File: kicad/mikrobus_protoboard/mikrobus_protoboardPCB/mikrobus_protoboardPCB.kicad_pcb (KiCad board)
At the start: 2 copper layers, 25.2 x 57.2 mm, 0 parts

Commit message: nets complete
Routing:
- net GND: track 0.00 -> 100.9 mm, vias 0 -> 17
- net 5V: track 0.00 -> 36.1 mm, vias 0 -> 8
- net 3V3: track 0.00 -> 36.0 mm, vias 0 -> 8
- net SDA: track 0.00 -> 7.69 mm, vias 0 -> 4
- net TX: track 0.00 -> 7.62 mm, vias 0 -> 4
- net SCL: track 0.00 -> 7.62 mm, vias 0 -> 4
- net SCK: track 0.00 -> 7.62 mm, vias 0 -> 4
- net RX: track 0.00 -> 7.62 mm, vias 0 -> 4
- net RST: track 0.00 -> 7.62 mm, vias 0 -> 4
- net PWD: track 0.00 -> 7.62 mm, vias 0 -> 4
- net MOSI: track 0.00 -> 7.62 mm, vias 0 -> 4
- net MISO: track 0.00 -> 7.62 mm, vias 0 -> 4
- net INT: track 0.00 -> 7.62 mm, vias 0 -> 4
- net CS: track 0.00 -> 7.62 mm, vias 0 -> 4
- net AN: track 0.00 -> 7.62 mm, vias 0 -> 4
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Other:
- board size 25.2 x 57.2 mm -> 25.8 x 57.5 mm

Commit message: protoboard ready
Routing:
- net GND: track 100.9 -> 0.37 mm
- added copper zone on F.Cu, net GND
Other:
- board size 25.8 x 57.5 mm -> 26.8 x 57.5 mm
- board text added: "3.3V"
- board text added: "5V"
- board text added: "AN"
- board text added: "CS"
- board text added: "GND"
- board text added: "INT"
- board text added: "PWD"
- board text added: "RST"
- board text added: "RX"
- board text added: "SCK"
- board text added: "SCL"
- board text added: "SDA"
- board text added: "SDI"
- board text added: "SDO"
- board text added: "TX"

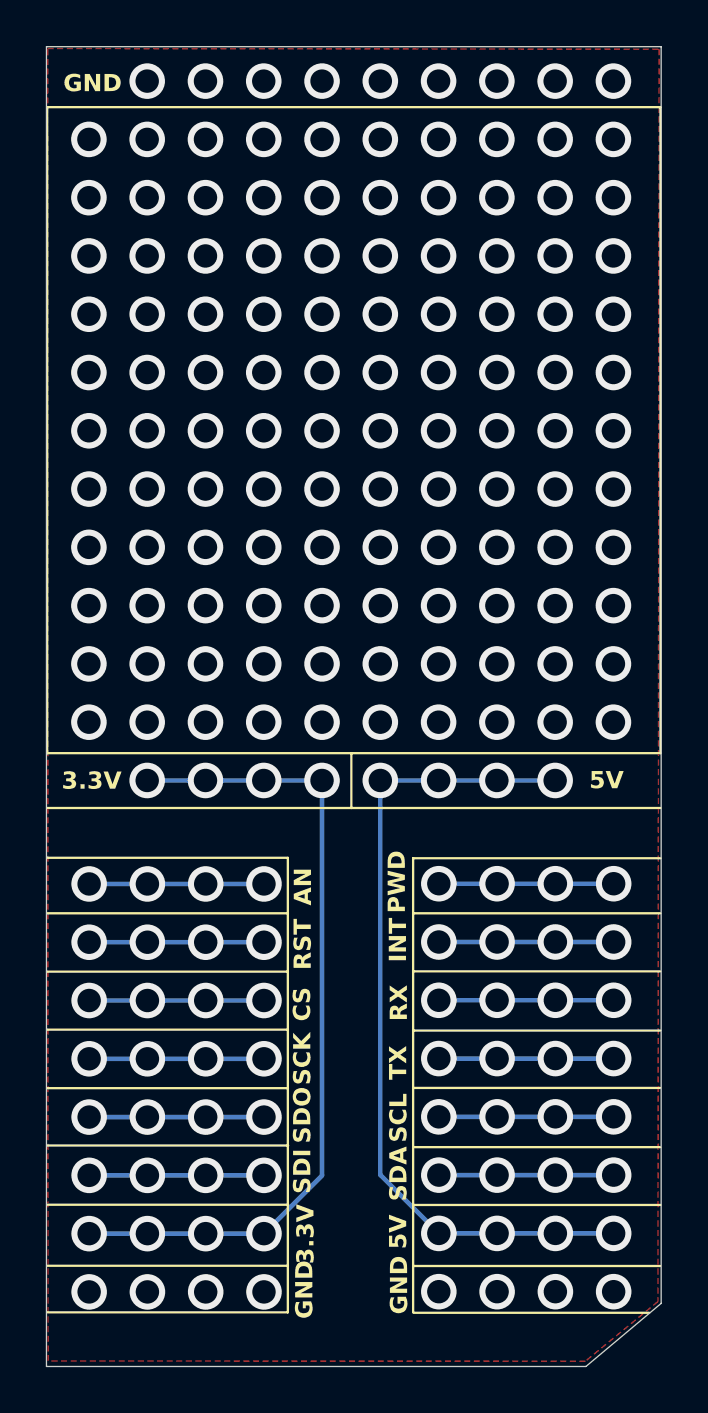
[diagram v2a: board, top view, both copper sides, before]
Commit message: MikroBUS logo added
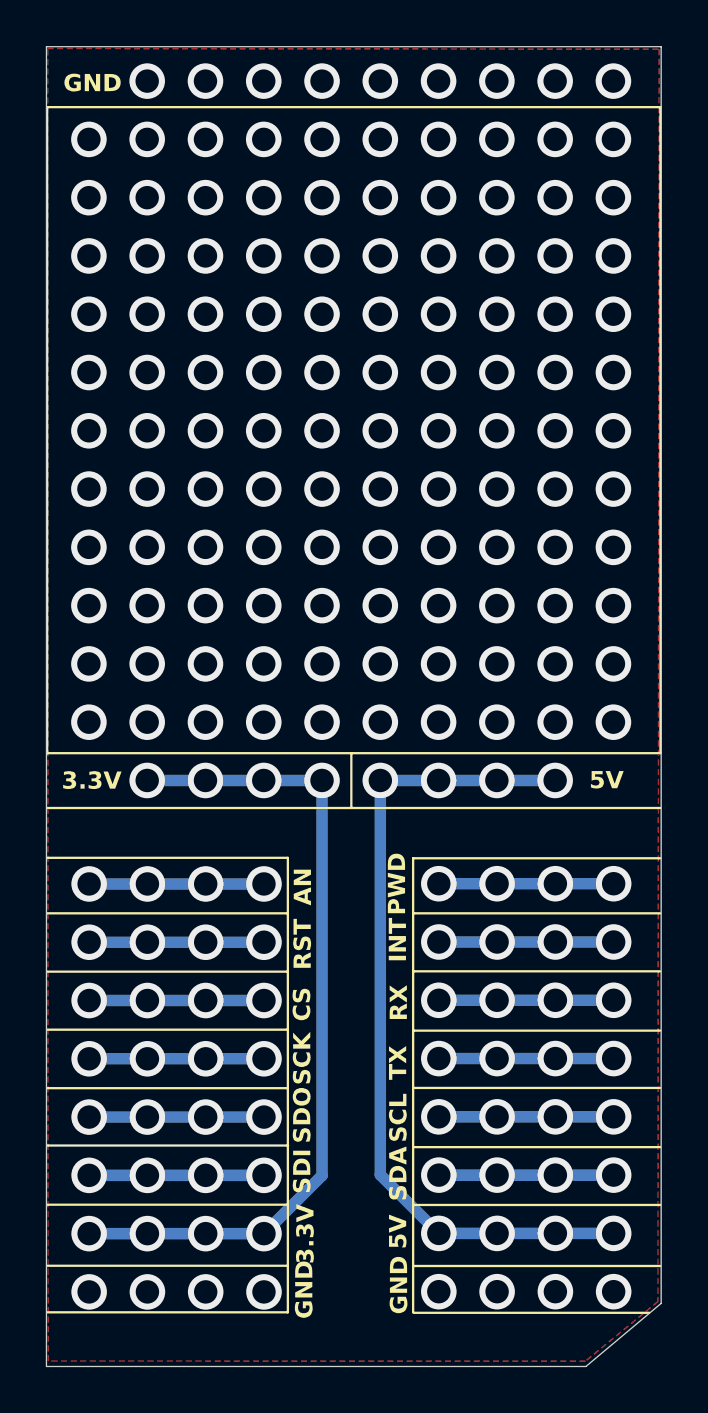
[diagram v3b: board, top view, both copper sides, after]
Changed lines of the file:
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@@
 	)
 	(gr_text "PWD"
-		(at 163.6 86.59 90)
+		(at 163.61 86.68 90)
 		(layer "F.SilkS")
 		(effects
@@
 		(start 164.98 103.09)
 		(end 164.99 103.08)
-		(width 0.2)
+		(width 0.5)
 		(layer "F.Cu")
 		(net 1)
@@
 		(start 164.75 103.08)
 		(end 164.99 103.08)
-		(width 0.2)
+		(width 0.5)
 		(layer "B.Cu")
 		(net 1)
@@
 		(start 164.87 103.08)
 		(end 164.99 103.08)
-		(width 0.2)
+		(width 0.5)
 		(layer "B.Cu")
 		(net 1)
@@
 		(start 159.9 98.02)
 		(end 157.37 100.55)
-		(width 0.2)
+		(width 0.5)
 		(layer "B.Cu")
 		(net 2)
@@
 		(start 154.82 80.8)
 		(end 157.36 80.8)
-		(width 0.2)
+		(width 0.5)
 		(layer "B.Cu")
 		(net 2)
@@
 		(start 157.37 100.55)
 		(end 154.83 100.55)
-		(width 0.2)
+		(width 0.5)
 		(layer "B.Cu")
 		(net 2)
@@
 		(start 152.29 100.55)
 		(end 149.75 100.55)
-		(width 0.2)
+		(width 0.5)
 		(layer "B.Cu")
 		(net 2)
@@
 		(start 154.83 100.55)
 		(end 152.29 100.55)
-		(width 0.2)
+		(width 0.5)
 		(layer "B.Cu")
 		(net 2)
@@
 		(start 152.28 80.8)
 		(end 154.82 80.8)
-		(width 0.2)
+		(width 0.5)
 		(layer "B.Cu")
 		(net 2)
@@
 		(start 157.36 80.8)
 		(end 159.9 80.8)
-		(width 0.2)
+		(width 0.5)
 		(layer "B.Cu")
 		(net 2)
@@
 		(start 159.9 80.8)
 		(end 159.9 98.02)
-		(width 0.2)
+		(width 0.5)
 		(layer "B.Cu")
 		(net 2)
@@
 		(start 172.61 100.54)
 		(end 172.59 100.54)
-		(width 0.2)
+		(width 0.5)
 		(layer "F.Cu")
 		(net 3)
@@
 		(start 172.59 100.54)
 		(end 172.57 100.52)
-		(width 0.2)
+		(width 0.5)
 		(layer "F.Cu")
 		(net 3)
@@
 		(start 172.57 100.52)
 		(end 172.55 100.54)
-		(width 0.2)
+		(width 0.5)
 		(layer "F.Cu")
 		(net 3)
@@
 		(start 162.44 80.8)
 		(end 164.98 80.8)
-		(width 0.2)
+		(width 0.5)
 		(layer "B.Cu")
 		(net 3)
@@
 		(start 167.53 100.54)
 		(end 170.07 100.54)
-		(width 0.2)
+		(width 0.5)
 		(layer "B.Cu")
 		(net 3)
@@
 		(start 170.07 100.54)
 		(end 172.61 100.54)
-		(width 0.2)
+		(width 0.5)
 		(layer "B.Cu")
 		(net 3)
@@
 		(start 164.99 100.54)
 		(end 167.53 100.54)
-		(width 0.2)
+		(width 0.5)
 		(layer "B.Cu")
 		(net 3)
@@
 		(start 167.52 80.8)
 		(end 170.06 80.8)
-		(width 0.2)
+		(width 0.5)
 		(layer "B.Cu")
 		(net 3)
@@
 		(start 162.44 97.99)
 		(end 164.99 100.54)
-		(width 0.2)
+		(width 0.5)
 		(layer "B.Cu")
 		(net 3)
@@
 		(start 164.98 80.8)
 		(end 167.52 80.8)
-		(width 0.2)
+		(width 0.5)
 		(layer "B.Cu")
 		(net 3)
@@
 		(start 162.44 80.8)
 		(end 162.44 97.99)
-		(width 0.2)
+		(width 0.5)
 		(layer "B.Cu")
 		(net 3)
@@
 		(start 167.53 85.3)
 		(end 170.07 85.3)
-		(width 0.2)
+		(width 0.5)
 		(layer "B.Cu")
 		(net 4)
@@
 		(start 164.99 85.3)
 		(end 167.53 85.3)
-		(width 0.2)
+		(width 0.5)
 		(layer "B.Cu")
 		(net 4)
@@
 		(start 170.07 85.3)
 		(end 172.61 85.3)
-		(width 0.2)
+		(width 0.5)
 		(layer "B.Cu")
 		(net 4)
@@
 		(start 164.99 87.84)
 		(end 167.53 87.84)
-		(width 0.2)
+		(width 0.5)
 		(layer "B.Cu")
 		(net 5)
@@
 		(start 167.53 87.84)
 		(end 170.07 87.84)
-		(width 0.2)
+		(width 0.5)
 		(layer "B.Cu")
 		(net 5)
@@
 		(start 170.07 87.84)
 		(end 172.61 87.84)
-		(width 0.2)
+		(width 0.5)
 		(layer "B.Cu")
 		(net 5)
@@
 		(start 167.53 90.38)
 		(end 170.07 90.38)
-		(width 0.2)
+		(width 0.5)
 		(layer "B.Cu")
 		(net 6)
@@
 		(start 164.99 90.38)
 		(end 167.53 90.38)
-		(width 0.2)
+		(width 0.5)
 		(layer "B.Cu")
 		(net 6)
@@
 		(start 170.07 90.38)
 		(end 172.61 90.38)
-		(width 0.2)
+		(width 0.5)
 		(layer "B.Cu")
 		(net 6)
@@
 		(start 172.61 92.92)
 		(end 170.07 92.92)
-		(width 0.2)
+		(width 0.5)
 		(layer "B.Cu")
 		(net 7)
@@
 		(start 167.53 92.92)
 		(end 164.99 92.92)
-		(width 0.2)
+		(width 0.5)
 		(layer "B.Cu")
 		(net 7)
@@
 		(start 170.07 92.92)
 		(end 167.53 92.92)
-		(width 0.2)
+		(width 0.5)
 		(layer "B.Cu")
 		(net 7)
@@
 		(start 164.99 95.46)
 		(end 167.53 95.46)
-		(width 0.2)
+		(width 0.5)
 		(layer "B.Cu")
 		(net 8)
@@
 		(start 172.61 95.46)
 		(end 170.07 95.46)
-		(width 0.2)
+		(width 0.5)
 		(layer "B.Cu")
 		(net 8)
@@
 		(start 167.53 95.46)
 		(end 170.07 95.46)
-		(width 0.2)
+		(width 0.5)
 		(layer "B.Cu")
 		(net 8)
@@
 		(start 167.57 98.04)
 		(end 167.53 98)
-		(width 0.2)
+		(width 0.5)
 		(layer "F.Cu")
 		(net 9)
@@
 		(start 170.07 98)
 		(end 170.07 98.03)
-		(width 0.2)
+		(width 0.5)
 		(layer "F.Cu")
 		(net 9)
@@
 		(start 170.07 98.03)
 		(end 170.08 98.04)
-		(width 0.2)
+		(width 0.5)
 		(layer "F.Cu")
 		(net 9)
@@
 		(start 167.53 98)
 		(end 164.99 98)
-		(width 0.2)
+		(width 0.5)
 		(layer "B.Cu")
 		(net 9)
@@
 		(start 172.61 98)
 		(end 170.07 98)
-		(width 0.2)
+		(width 0.5)
 		(layer "B.Cu")
 		(net 9)
@@
 		(start 170.07 98)
 		(end 167.53 98)
-		(width 0.2)
+		(width 0.5)
 		(layer "B.Cu")
 		(net 9)
@@
 		(start 152.29 98.01)
 		(end 154.83 98.01)
-		(width 0.2)
+		(width 0.5)
 		(layer "B.Cu")
 		(net 10)
@@
 		(start 154.83 98.01)
 		(end 157.37 98.01)
-		(width 0.2)
+		(width 0.5)
 		(layer "B.Cu")
 		(net 10)
@@
 		(start 149.75 98.01)
 		(end 152.29 98.01)
-		(width 0.2)
+		(width 0.5)
 		(layer "B.Cu")
 		(net 10)
@@
 		(start 152.29 95.47)
 		(end 154.83 95.47)
-		(width 0.2)
+		(width 0.5)
 		(layer "B.Cu")
 		(net 11)
@@
 		(start 154.83 95.47)
 		(end 157.37 95.47)
-		(width 0.2)
+		(width 0.5)
 		(layer "B.Cu")
 		(net 11)
@@
 		(start 149.75 95.47)
 		(end 152.29 95.47)
-		(width 0.2)
+		(width 0.5)
 		(layer "B.Cu")
 		(net 11)
@@
 		(start 152.29 92.93)
 		(end 154.83 92.93)
-		(width 0.2)
+		(width 0.5)
 		(layer "B.Cu")
 		(net 12)
@@
 		(start 149.75 92.93)
 		(end 152.29 92.93)
-		(width 0.2)
+		(width 0.5)
 		(layer "B.Cu")
 		(net 12)
@@
 		(start 157.37 92.93)
 		(end 154.83 92.93)
-		(width 0.2)
+		(width 0.5)
 		(layer "B.Cu")
 		(net 12)
@@
 		(start 154.83 90.39)
 		(end 157.37 90.39)
-		(width 0.2)
+		(width 0.5)
 		(layer "B.Cu")
 		(net 13)
@@
 		(start 149.75 90.39)
 		(end 152.29 90.39)
-		(width 0.2)
+		(width 0.5)
 		(layer "B.Cu")
 		(net 13)
@@
 		(start 152.29 90.39)
 		(end 154.83 90.39)
-		(width 0.2)
+		(width 0.5)
 		(layer "B.Cu")
 		(net 13)
@@
 		(start 152.29 87.85)
 		(end 149.75 87.85)
-		(width 0.2)
+		(width 0.5)
 		(layer "B.Cu")
 		(net 14)
@@
 		(start 152.29 87.85)
 		(end 154.83 87.85)
-		(width 0.2)
+		(width 0.5)
 		(layer "B.Cu")
 		(net 14)
@@
 		(start 157.37 87.85)
 		(end 154.83 87.85)
-		(width 0.2)
+		(width 0.5)
 		(layer "B.Cu")
 		(net 14)
@@
 		(start 152.29 85.31)
 		(end 154.83 85.31)
-		(width 0.2)
+		(width 0.5)
 		(layer "B.Cu")
 		(net 15)
@@
 		(start 154.83 85.31)
 		(end 157.37 85.31)
-		(width 0.2)
+		(width 0.5)
 		(layer "B.Cu")
 		(net 15)
@@
 		(start 149.75 85.31)
 		(end 152.29 85.31)
-		(width 0.2)
+		(width 0.5)
 		(layer "B.Cu")
 		(net 15)
